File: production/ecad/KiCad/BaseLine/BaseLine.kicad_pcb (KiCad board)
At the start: 4 copper layers, 107.2 x 119.5 mm, 122 parts, among them IC1 AP7362-33SP-13 (3.3V LDO), J1 VibeMotorConnector_1, J10 LoadCell1, J11 LoadCell2, J12 LoadCell3, J13 LoadCell4, J14 Power_to_Loadcell, J17 IMU_connector, J2 1332645, J3 Conn_01x02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

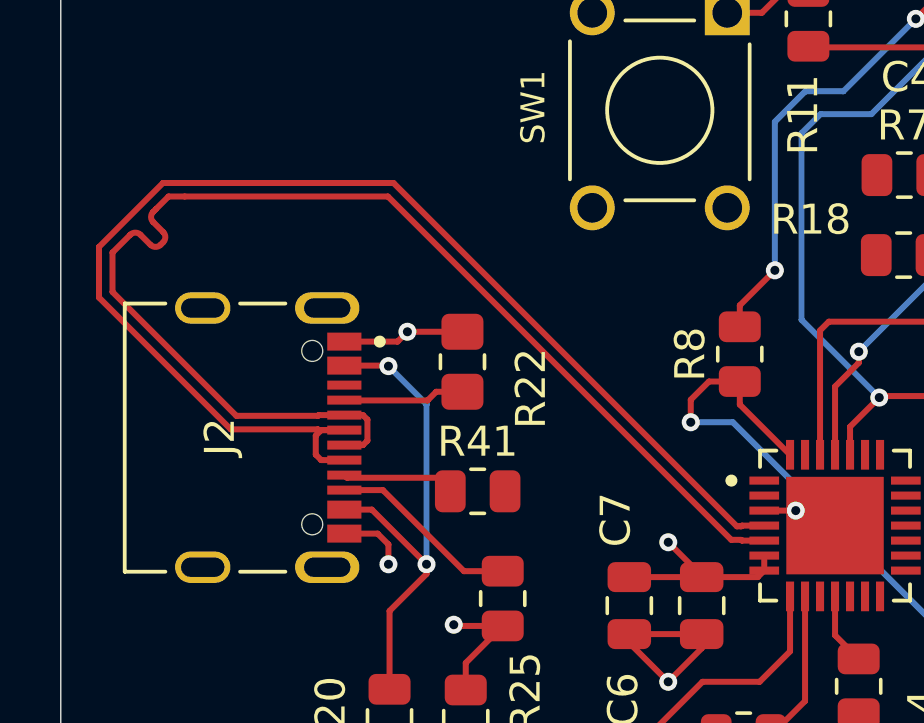
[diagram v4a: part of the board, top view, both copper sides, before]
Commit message: Modified routing of USB differential pair
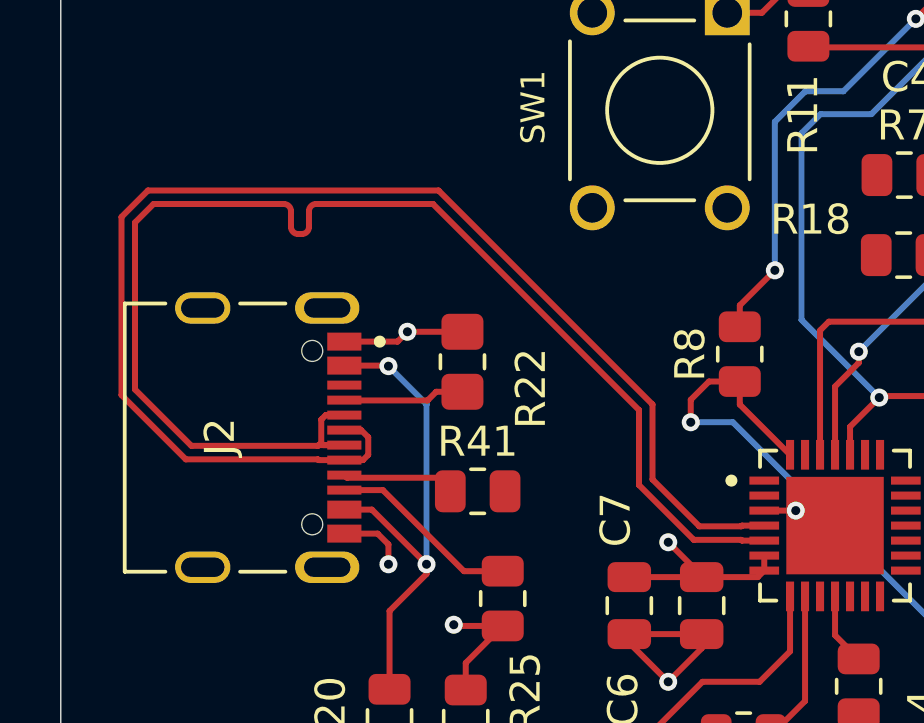
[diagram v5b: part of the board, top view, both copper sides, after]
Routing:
- net USB_D-: track 41.8 -> 44.6 mm
- net USB_D+: track 42.2 -> 44.5 mm
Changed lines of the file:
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@@
 	)
 	(segment
-		(start 63 119.695)
-		(end 63.183 119.512)
+		(start 74.225 121.1568)
+		(end 75.7882 122.72)
 		(width 0.2)
 		(layer "F.Cu")
@@
 	)
 	(segment
-		(start 77.182499 122.72)
-		(end 77.207499 122.695)
+		(start 67.0932 111.525)
+		(end 74.225 118.6568)
 		(width 0.2)
 		(layer "F.Cu")
@@
 	)
 	(segment
-		(start 63.097999 119.512)
-		(end 63.072999 119.487)
+		(start 58.6688 120.487)
+		(end 56.525 118.3432)
 		(width 0.2)
 		(layer "F.Cu")
@@
 	)
 	(segment
-		(start 77.0382 122.72)
-		(end 77.182499 122.72)
+		(start 77.207499 122.695)
+		(end 77.95 122.695)
 		(width 0.2)
 		(layer "F.Cu")
@@
 	)
 	(segment
-		(start 55.775 113.4068)
-		(end 57.9068 111.275)
+		(start 63.097999 120.512)
+		(end 63.072999 120.487)
 		(width 0.2)
 		(layer "F.Cu")
@@
 	)
 	(segment
-		(start 63.183 119.512)
-		(end 63.953 119.512)
+		(start 74.225 118.6568)
+		(end 74.225 121.1568)
+		(width 0.2)
+		(layer "F.Cu")
+		(net 20)
+	)
+	(segment
+		(start 64.75 120.335)
+		(end 64.75 119.75)
 		(width 0.2)
 		(layer "F.Cu")
@@
 	)
 	(segment
-		(start 63.183 120.512)
-		(end 63 120.329)
+		(start 64.573 120.512)
+		(end 64.75 120.335)
 		(width 0.2)
 		(layer "F.Cu")
@@
 	)
 	(segment
-		(start 65.5932 111.275)
-		(end 77.0382 122.72)
+		(start 77.182499 122.72)
+		(end 77.207499 122.695)
 		(width 0.2)
 		(layer "F.Cu")
@@
 	)
 	(segment
-		(start 63.072999 119.487)
-		(end 60.1688 119.487)
+		(start 56.525 112.4068)
+		(end 57.4068 111.525)
 		(width 0.2)
 		(layer "F.Cu")
@@
 	)
 	(segment
-		(start 63 120.329)
-		(end 63 119.695)
+		(start 64.75 119.75)
+		(end 64.512 119.512)
+		(width 0.2)
+		(layer "F.Cu")
+		(net 20)
+	)
+	(segment
+		(start 56.525 118.3432)
+		(end 56.525 112.4068)
 		(width 0.2)
 		(layer "F.Cu")
@@
 	)
 	(segment
-		(start 63.953 120.512)
-		(end 63.183 120.512)
+		(start 63.072999 120.487)
+		(end 58.6688 120.487)
 		(width 0.2)
 		(layer "F.Cu")
@@
 	)
 	(segment
-		(start 60.1688 119.487)
-		(end 55.775 115.0932)
+		(start 63.953 120.512)
+		(end 63.097999 120.512)
 		(width 0.2)
 		(layer "F.Cu")
@@
 	)
 	(segment
-		(start 57.9068 111.275)
-		(end 65.5932 111.275)
+		(start 64.512 119.512)
+		(end 63.953 119.512)
 		(width 0.2)
 		(layer "F.Cu")
@@
 	)
 	(segment
-		(start 63.953 119.512)
-		(end 63.097999 119.512)
+		(start 63.953 120.512)
+		(end 64.573 120.512)
 		(width 0.2)
 		(layer "F.Cu")
@@
 	)
 	(segment
-		(start 77.207499 122.695)
-		(end 77.95 122.695)
+		(start 57.4068 111.525)
+		(end 67.0932 111.525)
 		(width 0.2)
 		(layer "F.Cu")
@@
 	)
 	(segment
-		(start 55.775 115.0932)
-		(end 55.775 113.4068)
+		(start 75.7882 122.72)
+		(end 77.182499 122.72)
 		(width 0.2)
 		(layer "F.Cu")
@@
 	)
 	(segment
-		(start 77.207499 123.195)
-		(end 77.95 123.195)
+		(start 63.097999 120.012)
+		(end 63.072999 120.037)
 		(width 0.2)
 		(layer "F.Cu")
@@
 	)
 	(segment
-		(start 60.3552 119.037)
-		(end 56.225 114.9068)
+		(start 63.953 119.012)
+		(end 63.333 119.012)
 		(width 0.2)
 		(layer "F.Cu")
@@
 	)
 	(segment
-		(start 63.953 119.012)
-		(end 63.097999 119.012)
+		(start 63.072999 120.037)
+		(end 58.8552 120.037)
 		(width 0.2)
 		(layer "F.Cu")
@@
 	)
 	(segment
-		(start 57.914683 112.909882)
-		(end 57.581204 112.576403)
+		(start 63.953 120.012)
+		(end 63.097999 120.012)
 		(width 0.2)
 		(layer "F.Cu")
@@
 	)
 	(segment
-		(start 64.723 119.162)
-		(end 64.723 119.862)
+		(start 63.183 119.162)
+		(end 63.183 119.945)
 		(width 0.2)
 		(layer "F.Cu")
@@
 	)
 	(segment
-		(start 77.182499 123.17)
-		(end 77.207499 123.195)
+		(start 73.775 118.8432)
+		(end 73.775 121.3432)
 		(width 0.2)
 		(layer "F.Cu")
@@
 	)
 	(segment
-		(start 65.4068 111.725)
-		(end 76.8518 123.17)
+		(start 73.775 121.3432)
+		(end 75.6018 123.17)
 		(width 0.2)
 		(layer "F.Cu")
@@
 	)
 	(segment
-		(start 58.0932 111.725)
-		(end 58.634347 111.725)
+		(start 58.8552 120.037)
+		(end 56.975 118.1568)
 		(width 0.2)
 		(layer "F.Cu")
@@
 	)
 	(segment
-		(start 64.573 120.012)
-		(end 63.953 120.012)
+		(start 57.5932 111.975)
+		(end 61.934523 111.975)
 		(width 0.2)
 		(layer "F.Cu")
@@
 	)
 	(segment
-		(start 64.573 119.012)
-		(end 64.723 119.162)
+		(start 63.014523 111.975)
+		(end 63.134523 111.975)
 		(width 0.2)
 		(layer "F.Cu")
@@
 	)
 	(segment
-		(start 64.723 119.862)
-		(end 64.573 120.012)
+		(start 63.333 119.012)
+		(end 63.183 119.162)
 		(width 0.2)
 		(layer "F.Cu")
@@
 	)
 	(segment
-		(start 57.829831 113.334147)
-		(end 57.914683 113.249294)
+		(start 66.9068 111.975)
+		(end 73.775 118.8432)
 		(width 0.2)
 		(layer "F.Cu")
@@
 	)
 	(segment
-		(start 63.097999 119.012)
-		(end 63.072999 119.037)
+		(start 56.975 118.1568)
+		(end 56.975 112.5932)
 		(width 0.2)
 		(layer "F.Cu")
@@
 	)
 	(segment
-		(start 63.072999 119.037)
-		(end 60.3552 119.037)
+		(start 75.6018 123.17)
+		(end 77.182499 123.17)
 		(width 0.2)
 		(layer "F.Cu")
@@
 	)
 	(segment
-		(start 58.634347 111.725)
-		(end 65.4068 111.725)
+		(start 62.414523 112.975)
+		(end 62.534523 112.975)
 		(width 0.2)
 		(layer "F.Cu")
@@
 	)
 	(segment
-		(start 76.8518 123.17)
-		(end 77.182499 123.17)
+		(start 63.526801 111.975)
+		(end 66.9068 111.975)
 		(width 0.2)
 		(layer "F.Cu")
@@
 	)
 	(segment
-		(start 63.953 119.012)
-		(end 64.573 119.012)
+		(start 63.134523 111.975)
+		(end 63.526801 111.975)
 		(width 0.2)
 		(layer "F.Cu")
@@
 	)
 	(segment
-		(start 57.581204 112.236992)
-		(end 57.666059 112.15214)
+		(start 56.975 112.5932)
+		(end 57.5932 111.975)
 		(width 0.2)
 		(layer "F.Cu")
@@
 	)
 	(segment
-		(start 57.666059 112.15214)
-		(end 58.0932 111.725)
+		(start 62.774523 112.735)
+		(end 62.774523 112.215)
 		(width 0.2)
 		(layer "F.Cu")
@@
 	)
 	(segment
-		(start 57.156942 113.000669)
-		(end 57.49042 113.334147)
+		(start 77.207499 123.195)
+		(end 77.95 123.195)
 		(width 0.2)
 		(layer "F.Cu")
@@
 	)
 	(segment
-		(start 56.225 113.5932)
-		(end 56.817531 113.000669)
+		(start 77.182499 123.17)
+		(end 77.207499 123.195)
 		(width 0.2)
 		(layer "F.Cu")
@@
 	)
 	(segment
-		(start 56.225 114.9068)
-		(end 56.225 113.5932)
+		(start 63.25 120.012)
+		(end 63.953 120.012)
+		(width 0.2)
+		(layer "F.Cu")
+		(net 22)
+	)
+	(segment
+		(start 63.183 119.945)
+		(end 63.25 120.012)
+		(width 0.2)
+		(layer "F.Cu")
+		(net 22)
+	)
+	(segment
+		(start 62.174523 112.215)
+		(end 62.174523 112.735)
 		(width 0.2)
 		(layer "F.Cu")
@@
 	)
 	(arc
-		(start 56.817531 113.000669)
-		(mid 56.987236 112.930375)
-		(end 57.156942 113.000669)
+		(start 62.774523 112.215)
+		(mid 62.844817 112.045294)
+		(end 63.014523 111.975)
 		(width 0.2)
 		(layer "F.Cu")
@@
 	)
 	(arc
-		(start 57.914683 113.249294)
-		(mid 57.984978 113.079588)
-		(end 57.914683 112.909882)
+		(start 62.534523 112.975)
+		(mid 62.704229 112.904706)
+		(end 62.774523 112.735)
 		(width 0.2)
 		(layer "F.Cu")
@@
 	)
 	(arc
-		(start 57.49042 113.334147)
-		(mid 57.660126 113.404441)
-		(end 57.829831 113.334147)
+		(start 61.934523 111.975)
+		(mid 62.104229 112.045294)
+		(end 62.174523 112.215)
 		(width 0.2)
 		(layer "F.Cu")
@@
 	)
 	(arc
-		(start 57.581204 112.576403)
-		(mid 57.510909 112.406698)
-		(end 57.581204 112.236992)
+		(start 62.174523 112.735)
+		(mid 62.244817 112.904706)
+		(end 62.414523 112.975)
 		(width 0.2)
 		(layer "F.Cu")
@@
 		(base_line
 			(pts
-				(xy 56.817531 113.000669) (xy 58.0932 111.725) (xy 58.634347 111.725)
-			)
-		)
-		(base_line_coupled
-			(pts
-				(xy 56.499331 112.682469) (xy 56.541314 112.640486)
+				(xy 61.934523 111.975) (xy 63.526801 111.975)
 			)
 		)
 		(corner_radius_percent 80)
 		(end
-			(xy 58.634347 111.725)
+			(xy 63.526801 111.975)
 		)
 		(initial_side "right")
@@
 		(last_status "tuned")
 		(last_track_width 0.2)
-		(last_tuning "-0.0000 mm (tuned)")
+		(last_tuning "42.2617 mm (tuned)")
 		(max_amplitude 1)
 		(min_amplitude 0.2)
 		(min_spacing 0.6)
 		(origin
-			(xy 56.817531 113.000669)
+			(xy 61.934523 111.975)
 		)
 		(override_custom_rules no)
@@
 		(target_skew_max 0.1)
 		(target_skew_min -0.1)
-		(tuning_mode "diff_pair_skew")
-		(members 35e67941-3057-4296-a761-ab6c14639019 377821db-c05b-4173-8345-4874647289dc
-			7c1ecc44-d466-448b-b6df-a106ecb09915 87bd89d9-af18-403a-8fed-b34e1d967a2b
-			96791702-9422-4390-af3d-b136142de5ff 99be96b0-5a3d-42cd-aa66-a0320b2d976b
-			d30f9ecd-7bdb-4a31-8aa6-047814abcf36 e489546b-c40d-48c9-92e0-fd5be25856b1
-			e6188fb1-e934-4a07-b0bf-33a43e152b3a eae37d57-5308-44d7-aefb-393cbd5002ec
+		(tuning_mode "single")
+		(members 22bdf687-0881-49cf-875b-230021512f71 230a177f-7f46-4a25-8c17-b6b424c32a8c
+			46092c44-934a-44f0-b1f5-7a780095667a 6b0392f5-baf8-4caf-81de-7f78f653da30
+			743f4cfb-f6c2-4f61-b7cb-8ff53f45fee0 89cc199a-a526-4355-b16a-487128abc953
+			a4b42343-59c1-485f-b6fa-deaca3e56a5b ad2ba554-cdfd-406d-820b-c3cbb6c919bf
+			e6bd3a24-197d-4f4c-a4d0-60822814c510
 		)
 	)

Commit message: added mounting holes to main
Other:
- board size 107.2 x 119.5 mm -> 108.2 x 131.6 mm
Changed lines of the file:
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@@
 		)
 	)
+	(gr_circle
+		(center 60.71 164.56)
+		(end 62.96 164.56)
+		(stroke
+			(width 0.05)
+			(type default)
+		)
+		(fill none)
+		(layer "Edge.Cuts")
+	)
+	(gr_circle
+		(center 159.06 164.69)
+		(end 161.31 164.69)
+		(stroke
+			(width 0.05)
+			(type default)
+		)
+		(fill none)
+		(layer "Edge.Cuts")
+	)
+	(gr_circle
+		(center 158.71 40.94)
+		(end 160.96 40.94)
+		(stroke
+			(width 0.05)
+			(type default)
+		)
+		(fill none)
+		(layer "Edge.Cuts")
+	)
 	(gr_rect
-		(start 54.5 43.5)
-		(end 161.75 163)
+		(start 54.82 37.34)
+		(end 163.06 168.95)
+		(stroke
+			(width 0.05)
+			(type default)
+		)
+		(fill none)
+		(layer "Edge.Cuts")
+	)
+	(gr_circle
+		(center 61.64 41.62)
+		(end 63.89 41.62)
 		(stroke
 			(width 0.05)
@@
 		(polygon
 			(pts
-				(xy 52.88 40.64) (xy 53.13 171.38) (xy 171.25 170.25) (xy 168.5 40)
+				(xy 55.38 37.64) (xy 54.93 170.95) (xy 171.25 170.25) (xy 169.2 37.43)
 			)
 		)

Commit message: final changes
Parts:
- added ?: LOGO, LOGO, F.Cu at (137.0, 65.8)
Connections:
- J3 pad 1: +3.7V -> Battery3.7
- J7 pad 1: +3.7V -> Battery3.7
- J7 pad 4: +3.7V -> Battery3.7
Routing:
- net +3.7V: track 8.70 -> 22.6 mm, vias 82 -> 62
- net GND: track 159.1 -> 160.8 mm, vias 71 -> 72
- net USB_D-: track 44.6 -> 43.3 mm
- net USB_D+: track 44.5 -> 45.0 mm
- net Battery3.7: vias 0 -> 20
- added copper zone on In1.Cu, net Battery3.7
- added copper zone on B.Cu, net GND
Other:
- board text added: "Cat Menten Jani Passas Bryan Pitts Ava Gami"
